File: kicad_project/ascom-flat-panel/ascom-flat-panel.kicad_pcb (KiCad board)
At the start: 4 copper layers, 55 x 29.5 mm, 14 parts, among them J1 Servo, J3 JST-XH LED, Q1 IRLZ34N, Q2 IRLZ34N, U1 XIAO-SAMD21-DIP

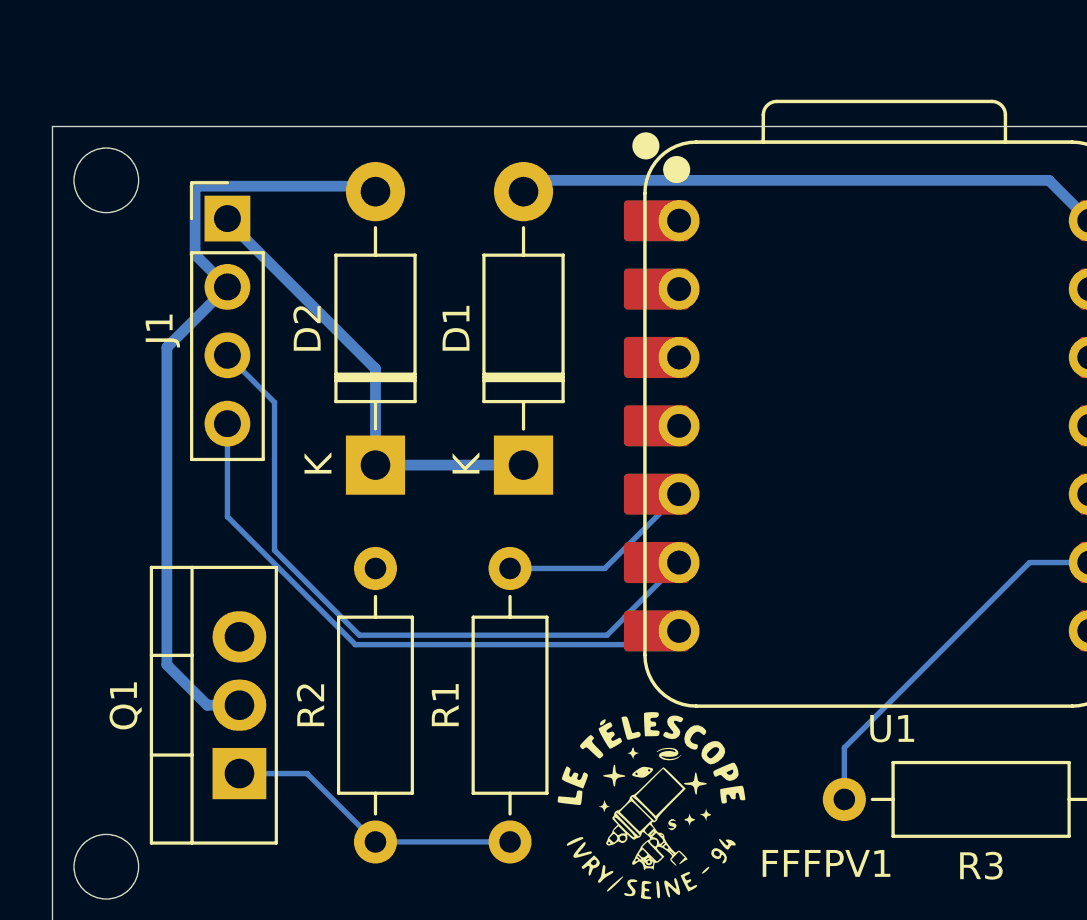
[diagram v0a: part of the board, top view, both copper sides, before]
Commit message: Ajout des VRAIES (a priori) design rules pcbway et petites modifications de routage pour s'y conformer
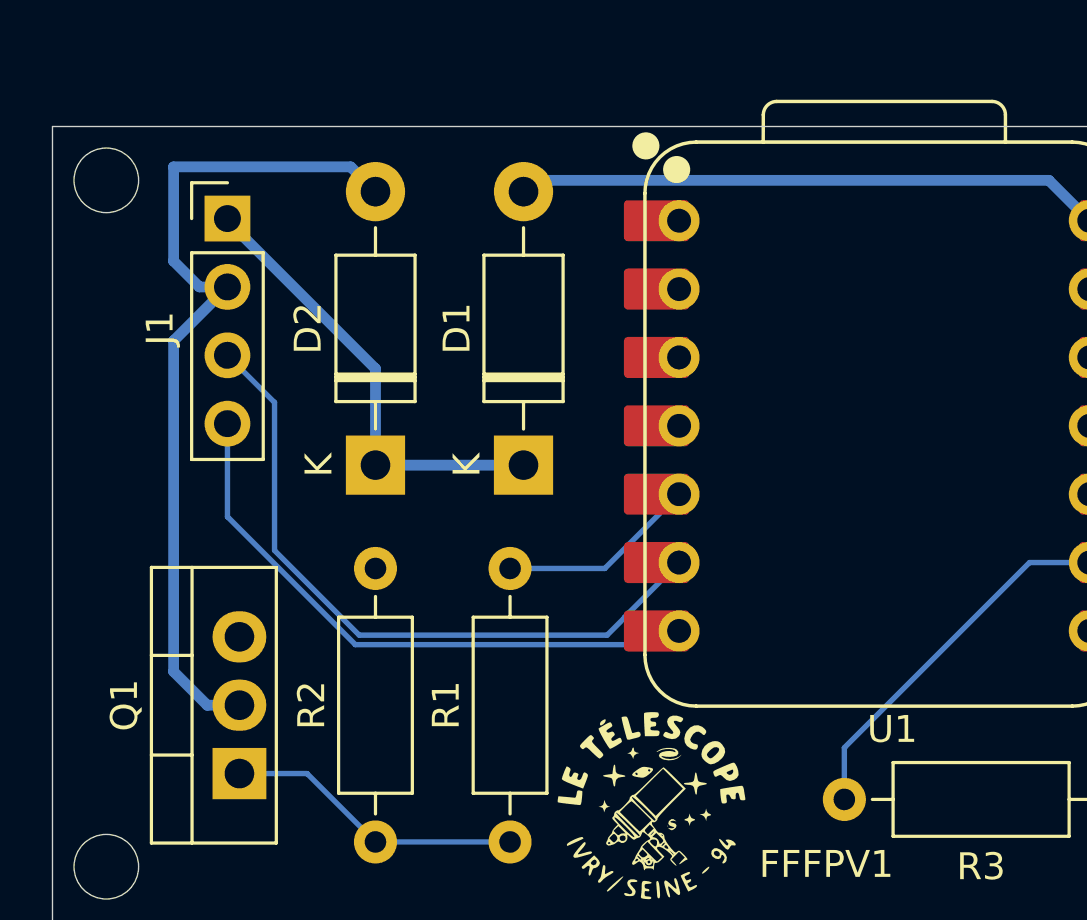
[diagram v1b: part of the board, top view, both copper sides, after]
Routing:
- net SERVO GND: track 29.3 -> 31.9 mm
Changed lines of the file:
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@@
 				(font
 					(size 1 1)
-					(thickness 0.1016)
+					(thickness 0.15)
 				)
 			)
@@
 	)
 	(segment
-		(start 102.299 74.259)
-		(end 103.5 75.46)
+		(start 109 71.92)
+		(end 108.08 71)
 		(width 0.4)
 		(layer "B.Cu")
@@
 	)
 	(segment
-		(start 102.299 71.719)
-		(end 102.299 74.259)
+		(start 102.75 91)
+		(end 101.5 89.75)
 		(width 0.4)
 		(layer "B.Cu")
@@
 	)
 	(segment
-		(start 108.799 71.719)
-		(end 102.299 71.719)
+		(start 101.5 77.46)
+		(end 103.5 75.46)
 		(width 0.4)
 		(layer "B.Cu")
@@
 	)
 	(segment
-		(start 101.25 89.5)
-		(end 101.25 77.71)
+		(start 108.08 71)
+		(end 101.5 71)
 		(width 0.4)
 		(layer "B.Cu")
@@
 	)
 	(segment
-		(start 109 71.92)
-		(end 108.799 71.719)
+		(start 102.46 75.46)
+		(end 103.5 75.46)
 		(width 0.4)
 		(layer "B.Cu")
@@
 	)
 	(segment
-		(start 101.25 77.71)
-		(end 103.5 75.46)
+		(start 101.5 89.75)
+		(end 101.5 77.46)
 		(width 0.4)
 		(layer "B.Cu")
@@
 	)
 	(segment
-		(start 102.75 91)
-		(end 101.25 89.5)
+		(start 101.5 74.5)
+		(end 102.46 75.46)
+		(width 0.4)
+		(layer "B.Cu")
+		(net 4)
+	)
+	(segment
+		(start 101.5 71)
+		(end 101.5 74.5)
 		(width 0.4)
 		(layer "B.Cu")

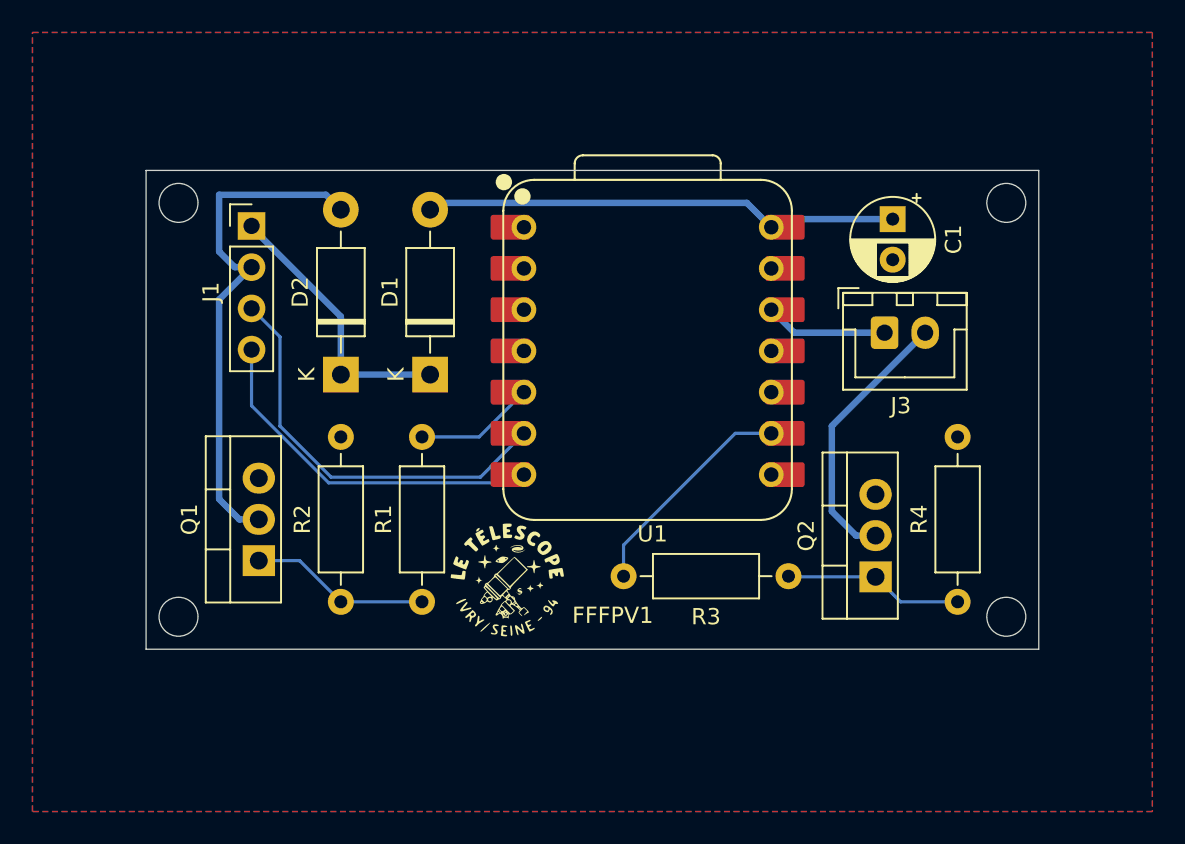
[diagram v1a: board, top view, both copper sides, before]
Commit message: réajustements de routage...
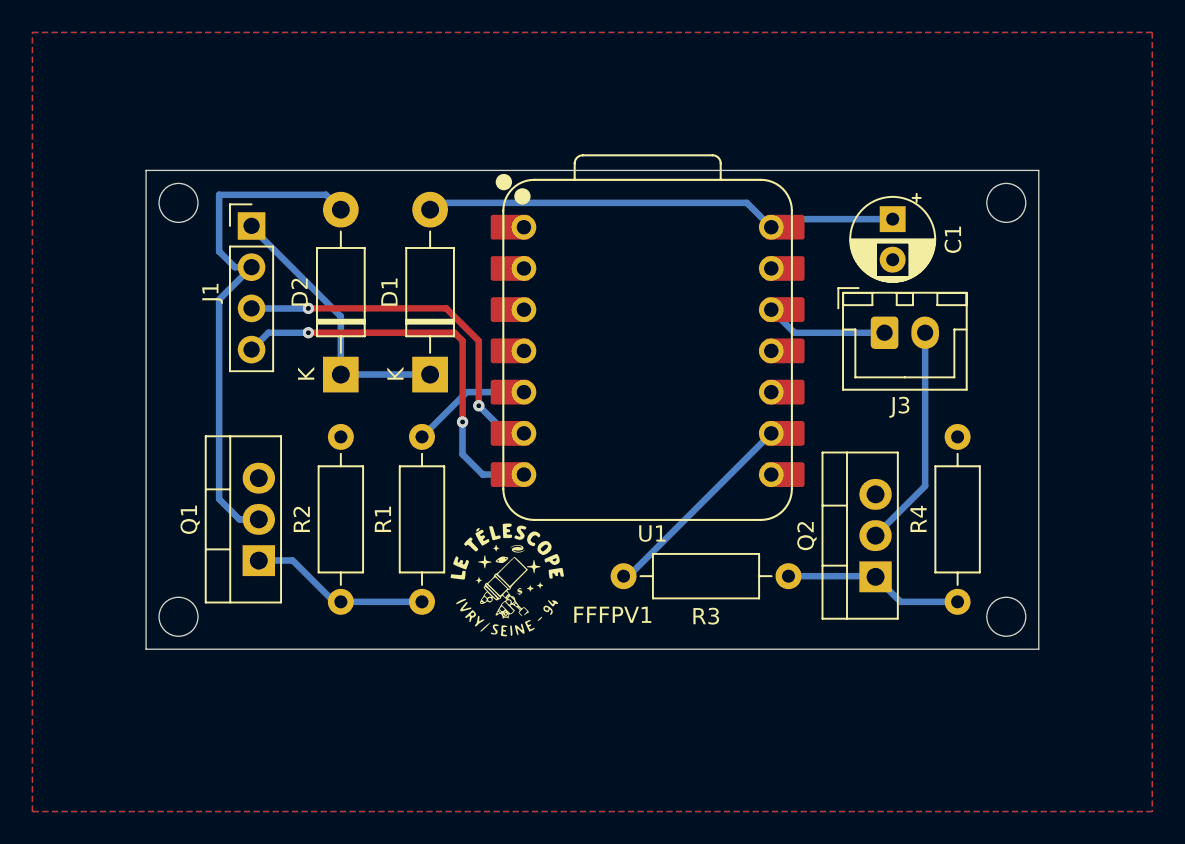
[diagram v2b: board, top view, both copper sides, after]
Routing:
- net SERVO POSITION CONTROL: track 25.9 -> 22.8 mm, vias 0 -> 2
- net Net-(J3-Pin_2): track 16.7 -> 13.8 mm
- net SERVO POSITION FEEDBACK: track 22.4 -> 24.9 mm, vias 0 -> 2
- net LED_STRIP_POWER_CONTROL: track 13.9 -> 12.7 mm
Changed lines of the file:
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@@
 	)
 	(segment
-		(start 119.77 88.75)
-		(end 108.25 88.75)
-		(width 0.2)
-		(layer "B.Cu")
-		(net 5)
-	)
-	(segment
-		(start 108.25 88.75)
-		(end 103.5 84)
-		(width 0.2)
+		(start 116 79.5)
+		(end 107 79.5)
+		(width 0.4)
+		(layer "F.Cu")
+		(net 5)
+	)
+	(segment
+		(start 116.5 85)
+		(end 116.5 80)
+		(width 0.4)
+		(layer "F.Cu")
+		(net 5)
+	)
+	(segment
+		(start 116.5 80)
+		(end 116 79.5)
+		(width 0.4)
+		(layer "F.Cu")
+		(net 5)
+	)
+	(via
+		(at 116.5 85)
+		(size 0.7)
+		(drill 0.3)
+		(layers "F.Cu" "B.Cu")
+		(net 5)
+	)
+	(via
+		(at 107 79.5)
+		(size 0.7)
+		(drill 0.3)
+		(layers "F.Cu" "B.Cu")
+		(net 5)
+	)
+	(segment
+		(start 116.5 85)
+		(end 116.5 87)
+		(width 0.4)
+		(layer "B.Cu")
+		(net 5)
+	)
+	(segment
+		(start 104.54 79.5)
+		(end 103.5 80.54)
+		(width 0.4)
 		(layer "B.Cu")
 		(net 5)
@@
 	(segment
 		(start 120.28 88.24)
-		(end 119.77 88.75)
-		(width 0.2)
-		(layer "B.Cu")
-		(net 5)
-	)
-	(segment
-		(start 103.5 84)
-		(end 103.5 80.54)
-		(width 0.2)
-		(layer "B.Cu")
-		(net 5)
+		(end 117.74 88.24)
+		(width 0.4)
+		(layer "B.Cu")
+		(net 5)
+	)
+	(segment
+		(start 117.74 88.24)
+		(end 116.5 87)
+		(width 0.4)
+		(layer "B.Cu")
+		(net 5)
+	)
+	(segment
+		(start 107 79.5)
+		(end 104.54 79.5)
+		(width 0.4)
+		(layer "B.Cu")
+		(net 5)
+	)
+	(segment
+		(start 117.5 84)
+		(end 117.5 80)
+		(width 0.4)
+		(layer "F.Cu")
+		(net 6)
+	)
+	(segment
+		(start 115.5 78)
+		(end 107 78)
+		(width 0.4)
+		(layer "F.Cu")
+		(net 6)
+	)
+	(segment
+		(start 117.5 80)
+		(end 115.5 78)
+		(width 0.4)
+		(layer "F.Cu")
+		(net 6)
+	)
+	(via
+		(at 107 78)
+		(size 0.7)
+		(drill 0.3)
+		(layers "F.Cu" "B.Cu")
+		(net 6)
+	)
+	(via
+		(at 117.5 84)
+		(size 0.7)
+		(drill 0.3)
+		(layers "F.Cu" "B.Cu")
+		(net 6)
 	)
 	(segment
@@
 	)
 	(segment
-		(start 117.601 88.399)
-		(end 118.25 87.75)
-		(width 0.2)
-		(layer "B.Cu")
-		(net 6)
-	)
-	(segment
-		(start 118.25 87.73)
-		(end 120.28 85.7)
-		(width 0.2)
-		(layer "B.Cu")
-		(net 6)
-	)
-	(segment
-		(start 103.5 78)
-		(end 105.25 79.75)
-		(width 0.2)
-		(layer "B.Cu")
-		(net 6)
-	)
-	(segment
-		(start 108.399 88.399)
-		(end 117.601 88.399)
-		(width 0.2)
-		(layer "B.Cu")
-		(net 6)
-	)
-	(segment
-		(start 105.25 85.25)
-		(end 108.399 88.399)
-		(width 0.2)
-		(layer "B.Cu")
-		(net 6)
-	)
-	(segment
-		(start 105.25 79.75)
-		(end 105.25 85.25)
-		(width 0.2)
-		(layer "B.Cu")
-		(net 6)
-	)
-	(segment
-		(start 118.25 87.75)
-		(end 118.25 87.73)
-		(width 0.15)
+		(start 119.2 85.7)
+		(end 117.5 84)
+		(width 0.4)
+		(layer "B.Cu")
+		(net 6)
+	)
+	(segment
+		(start 107 78)
+		(end 103.5 78)
+		(width 0.4)
+		(layer "B.Cu")
+		(net 6)
+	)
+	(segment
+		(start 120.28 85.7)
+		(end 119.2 85.7)
+		(width 0.4)
 		(layer "B.Cu")
 		(net 6)
@@
 	)
 	(segment
-		(start 139.25 85.25)
-		(end 145 79.5)
+		(start 145 88.945)
+		(end 141.945 92)
 		(width 0.4)
 		(layer "B.Cu")
@@
 	)
 	(segment
-		(start 140.75 92)
-		(end 139.25 90.5)
+		(start 145 79.5)
+		(end 145 88.945)
 		(width 0.4)
 		(layer "B.Cu")
 		(net 8)
-	)
-	(segment
-		(start 141.945 92)
-		(end 140.75 92)
-		(width 0.4)
-		(layer "B.Cu")
-		(net 8)
-	)
-	(segment
-		(start 139.25 90.5)
-		(end 139.25 85.25)
-		(width 0.4)
-		(layer "B.Cu")
-		(net 8)
-	)
-	(segment
-		(start 106.46 93.54)
-		(end 109 96.08)
-		(width 0.2)
-		(layer "B.Cu")
-		(net 9)
 	)
 	(segment
 		(start 114 96.08)
 		(end 109 96.08)
-		(width 0.2)
-		(layer "B.Cu")
-		(net 9)
-	)
-	(segment
-		(start 103.945 93.54)
-		(end 106.46 93.54)
-		(width 0.2)
+		(width 0.4)
+		(layer "B.Cu")
+		(net 9)
+	)
+	(segment
+		(start 106.04 93.54)
+		(end 103.945 93.54)
+		(width 0.4)
+		(layer "B.Cu")
+		(net 9)
+	)
+	(segment
+		(start 108.58 96.08)
+		(end 106.04 93.54)
+		(width 0.4)
+		(layer "B.Cu")
+		(net 9)
+	)
+	(segment
+		(start 109 96.08)
+		(end 108.58 96.08)
+		(width 0.4)
 		(layer "B.Cu")
 		(net 9)
@@
 	)
 	(segment
+		(start 141.905 94.5)
+		(end 141.945 94.54)
+		(width 0.4)
+		(layer "B.Cu")
+		(net 10)
+	)
+	(segment
+		(start 136.58 94.5)
+		(end 141.905 94.5)
+		(width 0.4)
+		(layer "B.Cu")
+		(net 10)
+	)
+	(segment
+		(start 141.945 94.54)
+		(end 142.54 94.54)
+		(width 0.2)
+		(layer "B.Cu")
+		(net 10)
+	)
+	(segment
+		(start 141.485 95)
+		(end 141.945 94.54)
+		(width 0.2)
+		(layer "B.Cu")
+		(net 10)
+	)
+	(segment
+		(start 143.485 96.08)
+		(end 141.945 94.54)
+		(width 0.4)
+		(layer "B.Cu")
+		(net 10)
+	)
+	(segment
 		(start 147 96.08)
 		(end 143.485 96.08)
-		(width 0.2)
-		(layer "B.Cu")
-		(net 10)
-	)
-	(segment
-		(start 141.945 94.54)
-		(end 142.54 94.54)
-		(width 0.2)
-		(layer "B.Cu")
-		(net 10)
-	)
-	(segment
-		(start 141.485 95)
-		(end 141.945 94.54)
-		(width 0.2)
-		(layer "B.Cu")
-		(net 10)
-	)
-	(segment
-		(start 141.945 94.54)
-		(end 136.62 94.54)
-		(width 0.2)
-		(layer "B.Cu")
-		(net 10)
-	)
-	(segment
-		(start 143.485 96.08)
-		(end 141.945 94.54)
-		(width 0.2)
+		(width 0.4)
 		(layer "B.Cu")
 		(net 10)
@@
 	)
 	(segment
-		(start 117.52 85.92)
-		(end 120.28 83.16)
-		(width 0.2)
+		(start 120.28 83.16)
+		(end 116.76 83.16)
+		(width 0.4)
 		(layer "B.Cu")
 		(net 11)
 	)
 	(segment
-		(start 114 85.92)
-		(end 117.52 85.92)
-		(width 0.2)
+		(start 116.76 83.16)
+		(end 114 85.92)
+		(width 0.4)
 		(layer "B.Cu")
 		(net 11)
 	)
 	(segment
-		(start 126.42 92.58)
-		(end 133.3 85.7)
-		(width 0.2)
+		(start 135.52 85.7)
+		(end 126.72 94.5)
+		(width 0.4)
 		(layer "B.Cu")
 		(net 12)
 	)
 	(segment
-		(start 133.3 85.7)
-		(end 135.52 85.7)
-		(width 0.2)
+		(start 126.72 94.5)
+		(end 126.42 94.5)
+		(width 0.4)
 		(layer "B.Cu")
 		(net 12)
-	)
-	(segment
-		(start 126.42 94.5)
-		(end 126.42 92.58)
-		(width 0.2)
-		(layer "B.Cu")
-		(net 12)

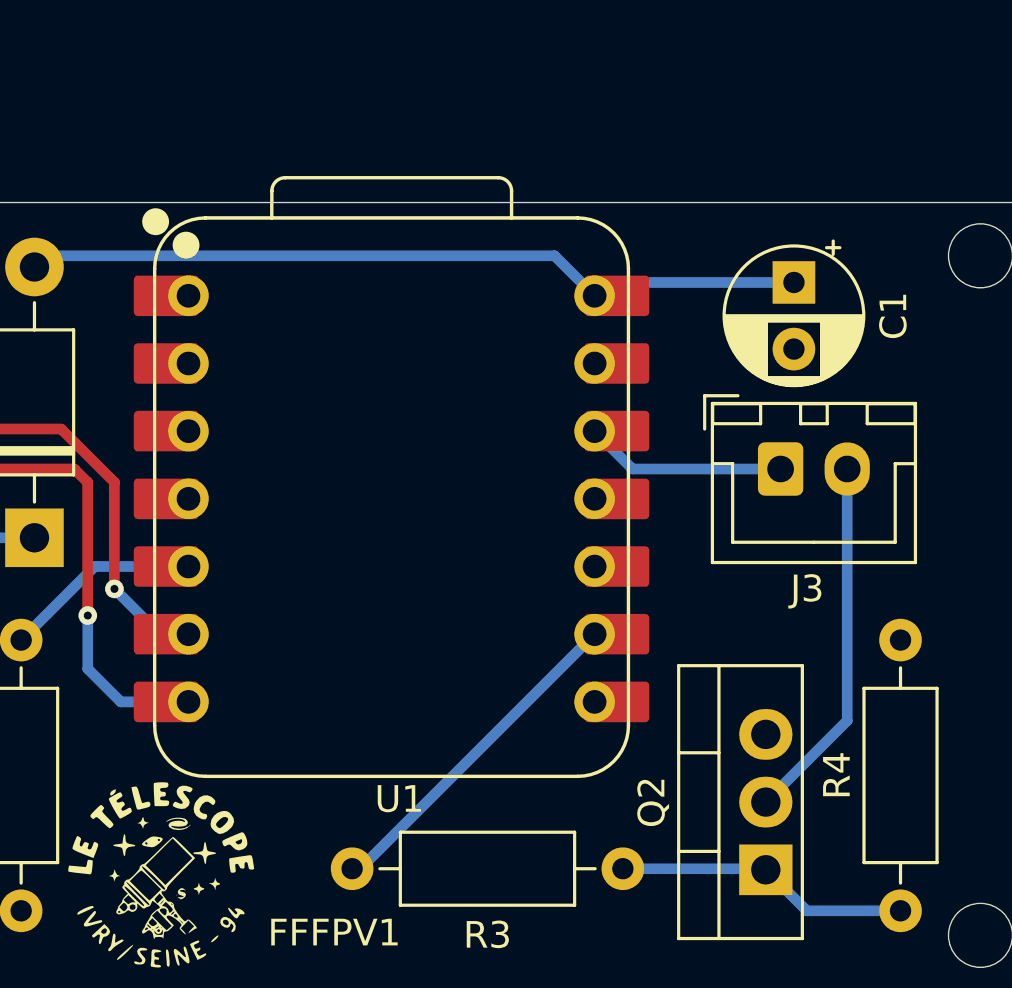
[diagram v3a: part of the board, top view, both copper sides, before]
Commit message: [kicad] - modification du pcb pour l'alimentation des LEDs en cohérence avec le schéma + réparation portabilité modèle 3D...
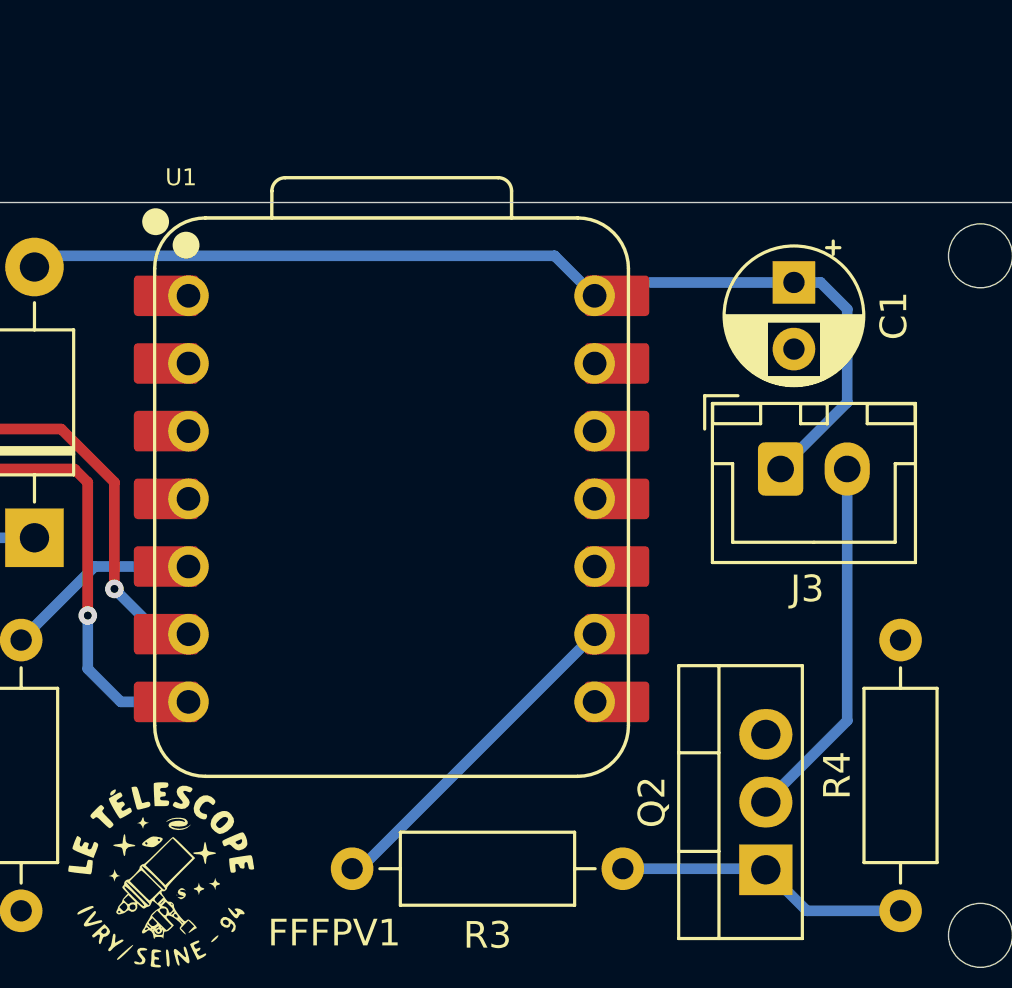
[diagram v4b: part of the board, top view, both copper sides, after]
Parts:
- U1: footprint Seeeduino XIAO:XIAO-SAMD21-DIP -> SEEED_STUDIO:XIAO-SAMD21-DIP
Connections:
- J3 pad 1: +3V3 -> +5V
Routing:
- net +5V: track 29.5 -> 39.0 mm
- net +3V3: track 7.57 -> 0.00 mm
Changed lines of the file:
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@@
 	(net 18 "unconnected-(U1-PB09_A7_D7_RX-Pad8)")
 	(net 19 "unconnected-(U1-PA6_A10_D10_MOSI-Pad11)")
-	(footprint "Seeeduino XIAO:XIAO-SAMD21-DIP"
+	(footprint "SEEED_STUDIO:XIAO-SAMD21-DIP"
 		(layer "F.Cu")
 		(at 128 80.5575)
 		(property "Reference" "U1"
-			(at 0.2 11.3425 0)
+			(at -8 -12 0)
 			(unlocked yes)
 			(layer "F.SilkS")
 			(effects
 				(font
-					(size 1 1)
-					(thickness 0.15)
+					(size 0.635 0.635)
+					(thickness 0.1016)
 				)
 			)
@@
 		)
 		(model "${AMZPATH}/3dmodels/AMz3D.3dshapes/Seeeduino XIAO SAMD21 v4.step"
-			(hide yes)
 			(offset
 				(xyz 0 0 0)
@@
 			)
 		)
-		(model "${SEEEDUINO_XIAO}/Seeeduino XIAO SAMD21 v4.step"
-			(offset
-				(xyz 0 0 0)
-			)
-			(scale
-				(xyz 1 1 1)
-			)
-			(rotate
-				(xyz -0 -0 -90)
-			)
-		)
 		(model "${KIPRJMOD}/Seeeduino XIAO SAMD21 v4.step"
 			(offset
@@
 			(remove_unused_layers no)
 			(roundrect_rratio 0.147059)
-			(net 7 "+3V3")
+			(net 2 "+5V")
 			(pinfunction "Pin_1")
 			(pintype "passive")
@@
 	)
 	(segment
+		(start 145 73.5)
+		(end 145 77)
+		(width 0.4)
+		(layer "B.Cu")
+		(net 2)
+	)
+	(segment
+		(start 143 72.5)
+		(end 144 72.5)
+		(width 0.4)
+		(layer "B.Cu")
+		(net 2)
+	)
+	(segment
+		(start 145 77)
+		(end 142.5 79.5)
+		(width 0.4)
+		(layer "B.Cu")
+		(net 2)
+	)
+	(segment
 		(start 143 72.5)
 		(end 136.02 72.5)
@@
 	)
 	(segment
+		(start 144 72.5)
+		(end 145 73.5)
+		(width 0.4)
+		(layer "B.Cu")
+		(net 2)
+	)
+	(segment
 		(start 114.92 71.5)
 		(end 114.5 71.92)
@@
 	)
 	(segment
-		(start 142.5 79.5)
-		(end 136.94 79.5)
-		(width 0.4)
-		(layer "B.Cu")
-		(net 7)
-	)
-	(segment
-		(start 136.94 79.5)
-		(end 135.52 78.08)
-		(width 0.4)
-		(layer "B.Cu")
-		(net 7)
-	)
-	(segment
